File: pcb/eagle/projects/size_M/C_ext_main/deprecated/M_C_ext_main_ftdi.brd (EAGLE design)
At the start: 17 parts

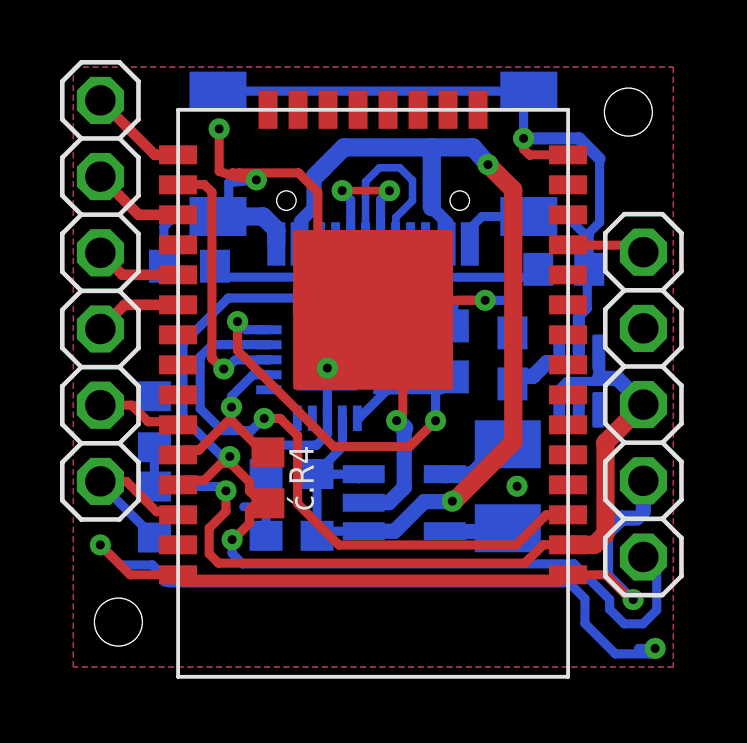
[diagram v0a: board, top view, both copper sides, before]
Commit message: version 8 main changes * ideal diode separated 3v3 DC-DC to protect it from back current * smaller package of ina 219 * usage of tssop attiny v2 in adapter * and change of PA5 to PB2 with ^ and ~ (originally used for shield power switch - now PB3) * step motor shield * out signal for BT module
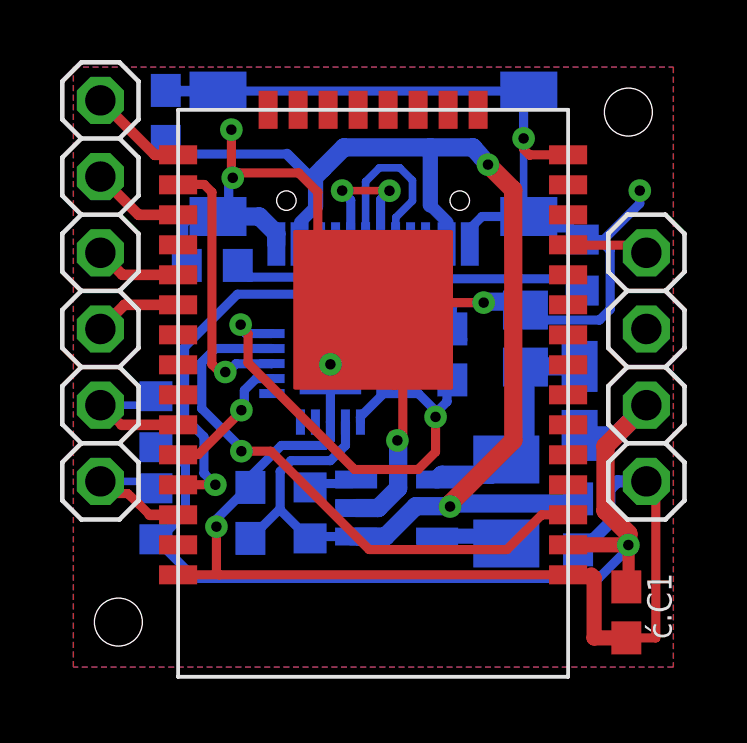
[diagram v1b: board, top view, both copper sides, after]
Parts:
- removed JP2: (no value), pinhead2:1X05
- removed ć.R4: 2k2, rcl:R0603
- removed ć.U4: LM66100DCKR, LM66100DCKR:SOT65P210X110-6N
- added JP1: (no value), pinhead2:1X04
- added ć.C1: 100n, rcl:C0603
- added ć.C6: 10nF, rcl:C0603
- added ć.D1: SHOTKY_2.8, hugo:SHOTKY_2.8
- added ć.R3: 100k, rcl:R0603
- ć.C3: value 10u -> 22u; device rcl:C0603 -> rcl:C0805
- moved ć.C5 9.56 mm to (17.3, 5.26), turned to 90 degrees
- moved ć.C4 1.89 mm to (6.40, 5.64), turned to 90 degrees
- moved ć.C3 0.79 mm to (15.6, 11.5)
- moved ć.R6 0.76 mm to (5.13, 13.9)
- moved ć.R5 0.63 mm to (17.5, 13.9), turned to 270 degrees
- moved ć.L1 0.51 mm to (14.9, 6.02)
- moved ć.U3 0.31 mm to (11.3, 5.80)
- moved ć.U2 0.16 mm to (9.07, 10.6)
- moved ć.C2 0.11 mm to (13.1, 10.9)
- moved ć.R1 0.08 mm to (3.25, 5.61), turned to 270 degrees
- moved ć.R2 0.05 mm to (3.25, 8.68)
- renumbered ć.U1 to C.U1
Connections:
- removed net VCC1: ć.C3.1, ć.L1.2, ć.U3.BP, ć.U4.1
- new net N$11: ć.R3.1, ć.U3.SHDN
- new net N$5: ć.C3.1, ć.D1.A, ć.L1.2, ć.U3.BP
- net GND: now also JP1.4, ć.C1.2, ć.C6.1; no longer JP2.4, ć.U4.2
- net PA5: now also JP1.1; no longer JP2.1
- net RX/TX: no longer JP2.5, ć.R4.1
- net TX/RX: no longer ć.R4.2
- net VCC: now also JP1.3, ć.C1.1, ć.D1.K; no longer JP2.3, ć.U4.3, ć.U4.6
- net VUSB: now also ć.C6.2, ć.R3.2; no longer ć.U3.SHDN
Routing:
- net RX/TX: track 33.6 -> 11.3 mm, vias 2 -> 1
- net GND: track 132.6 -> 115.2 mm, vias 10 -> 8
- net VUSB: track 36.3 -> 48.2 mm
- net N$5: track 0.00 -> 7.74 mm
- net VCC1: track 6.92 -> 0.00 mm
- net VCC: track 30.5 -> 33.7 mm
- net TX/RX: track 6.80 -> 4.53 mm
- net N$4: track 4.91 -> 6.75 mm
- net N$11: track 0.00 -> 1.64 mm
- net RESET: track 20.4 -> 18.8 mm
- net SCL: track 5.78 -> 4.99 mm
- net N$3: track 5.57 -> 4.80 mm
